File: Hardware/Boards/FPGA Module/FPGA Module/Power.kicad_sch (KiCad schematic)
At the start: 102 parts, among them Q2 IRLML6244, Q3 IRLML6244, Q4 IRLML6244, U10 INA700AYWFR, U12 INA700AYWFR, U2 INA700AYWFR, U22 TPSM33625RDNR, U23 TPSM33625RDNR, U24 TPSM33625RDNR, U3 AOZ2369QI-11, U4 TPS62933O, U7 INA700AYWFR, U8 INA236

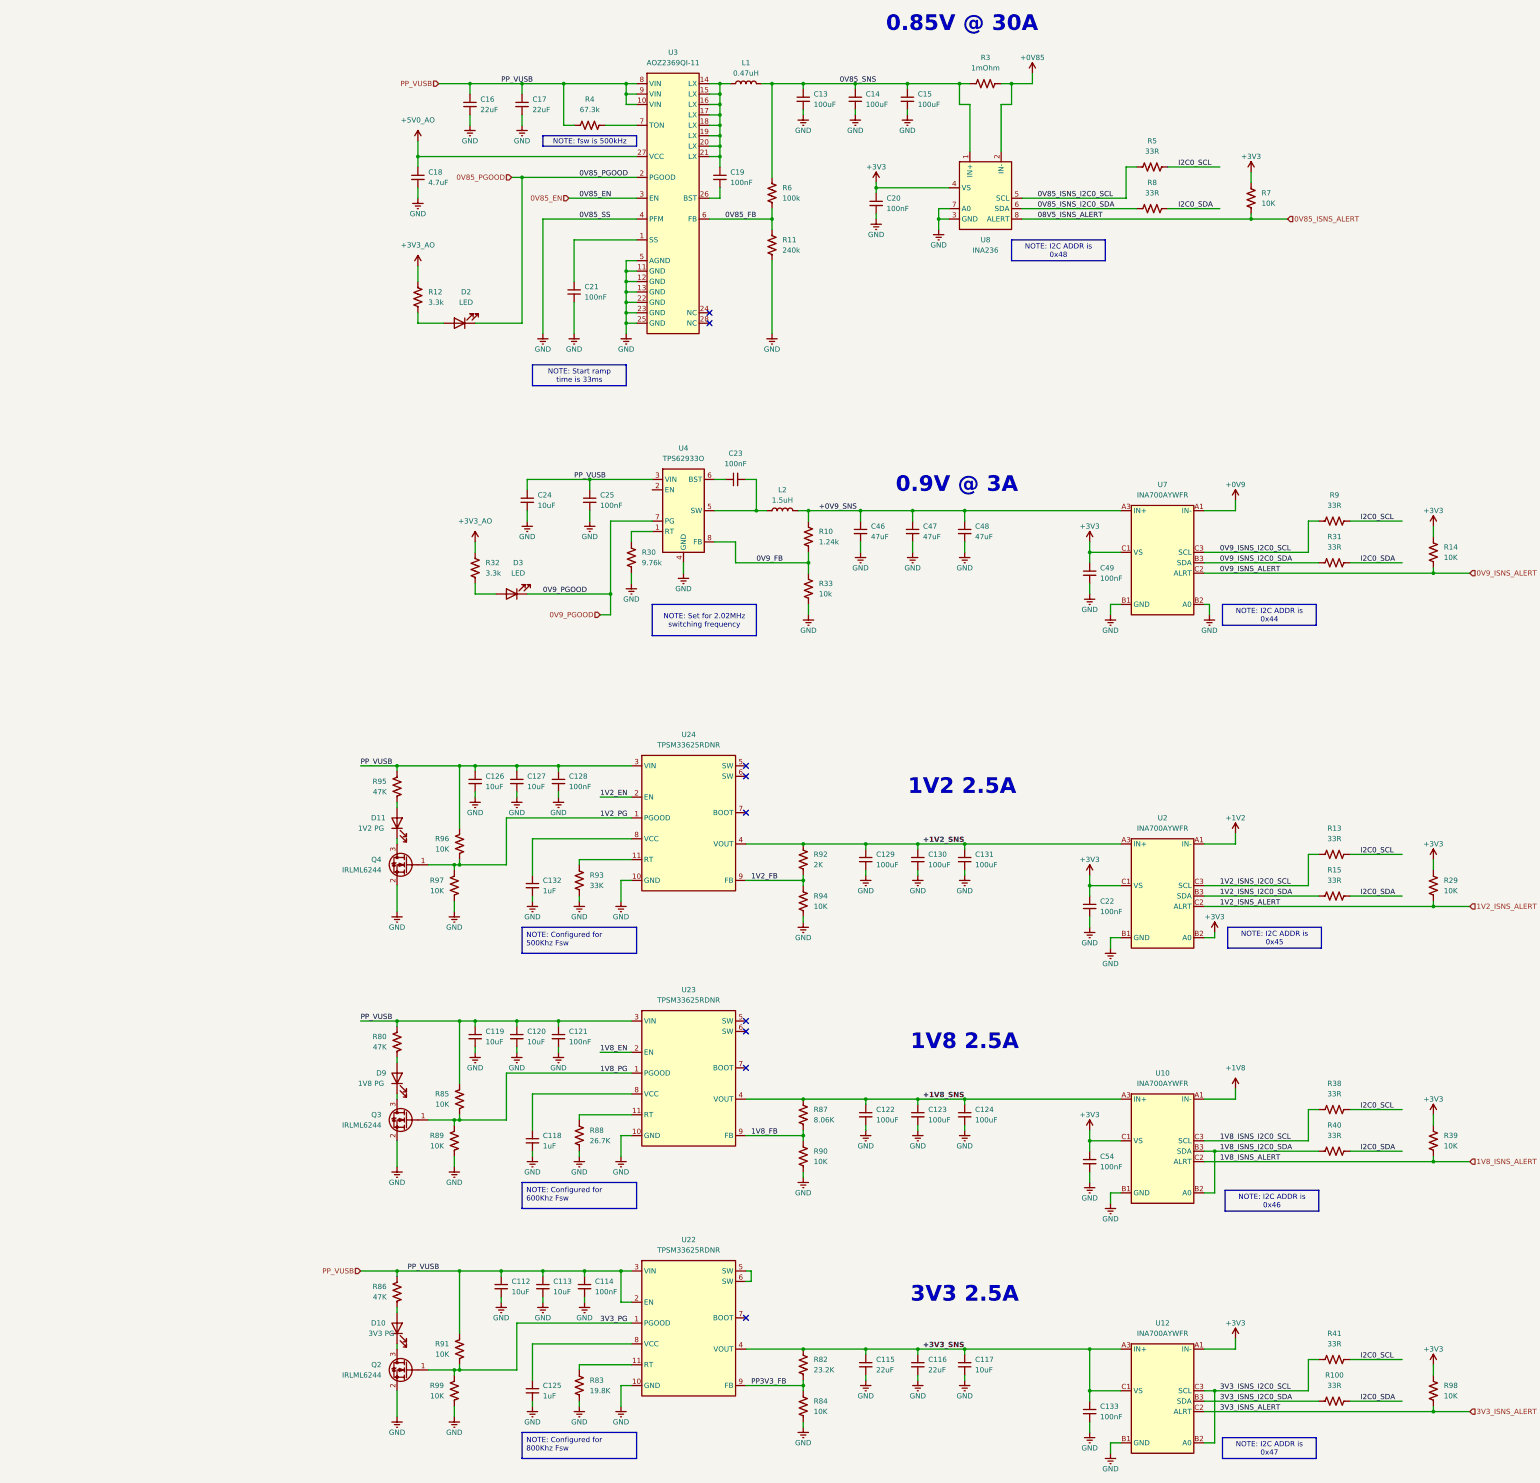
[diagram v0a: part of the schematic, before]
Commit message: updated fpga module schematics
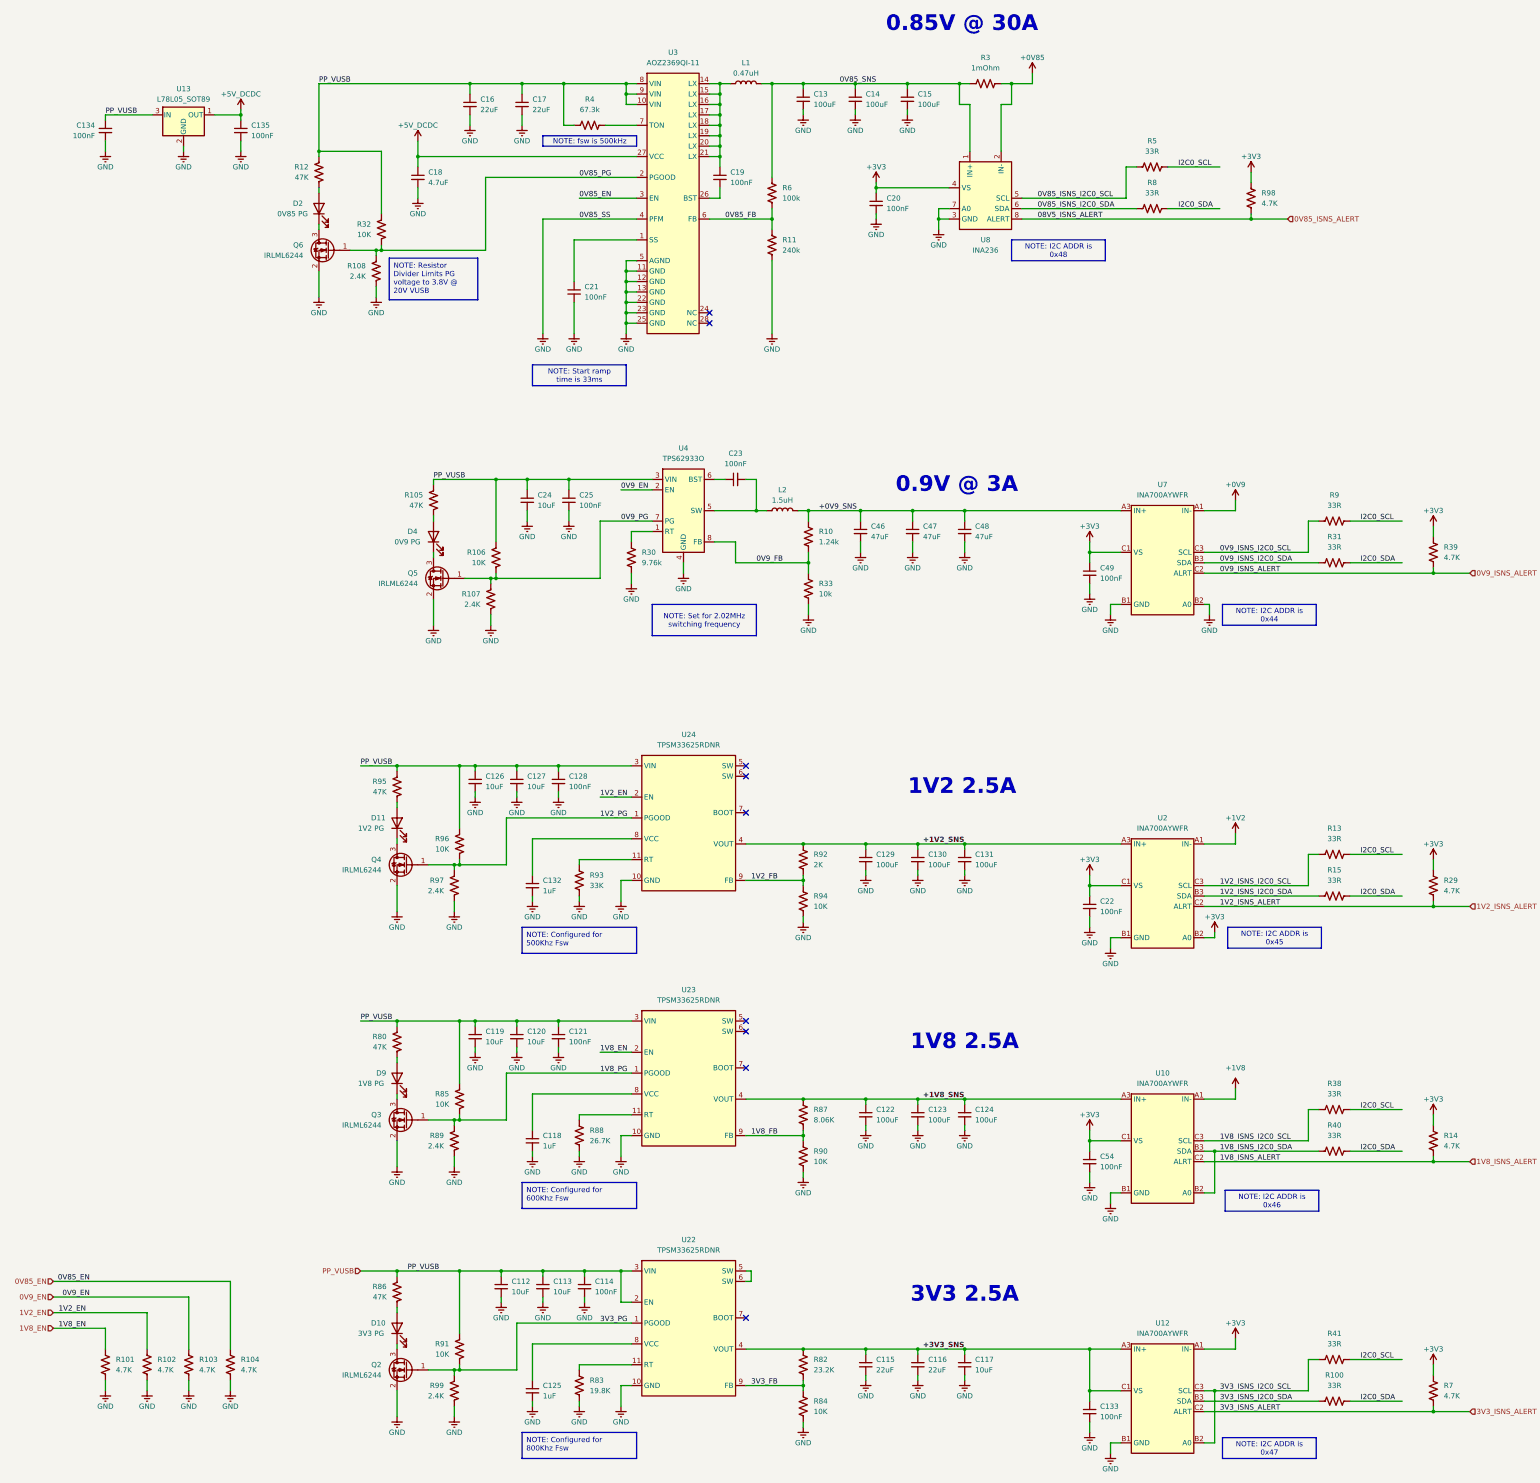
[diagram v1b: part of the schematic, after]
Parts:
- removed D3: LED, LED_SMD:LED_0603_1608Metric, symbol Device:LED
- added C134, C135: 100nF, Capacitor_SMD:C_0402_1005Metric, symbol Device:C_Small
- added D4: 0V9 PG, LED_SMD:LED_0603_1608Metric, symbol Device:LED
- added Q5, Q6: IRLML6244, Package_TO_SOT_SMD:SOT-23, symbol Transistor_FET:IRLML6244
- added R101, R102, R103, R104: 4.7K, Resistor_SMD:R_0402_1005Metric, symbol Device:R_US
- added R105: 47K, Resistor_SMD:R_0402_1005Metric, symbol Device:R_US
- added R106: 10K, Resistor_SMD:R_0402_1005Metric, symbol Device:R_US
- added R107, R108: 2.4K, Resistor_SMD:R_0402_1005Metric, symbol Device:R_US
- added U13: L78L05_SOT89, Package_TO_SOT_SMD:SOT-89-3, symbol Regulator_Linear:L78L05_SOT89
- D2: value LED -> 0V85 PG
- R12: value 3.3k -> 47K
- R14, R29, R39, R7, R98: value 10K -> 4.7K
- R32: value 3.3k -> 10K
- R89, R97, R99: value 10K -> 2.4K
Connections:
- net 0V85_EN: now also R104.2
- net 0V85_ISNS_ALERT: now also R98.1; no longer R7.1
- net 0V9_ISNS_ALERT: now also R39.1; no longer R14.1
- net 1V2_EN: now also R102.2
- net 1V8_EN: now also R101.2
- net 1V8_ISNS_ALERT: now also R14.1; no longer R39.1
- net 3V3_ISNS_ALERT: now also R7.1; no longer R98.1
- net GND: now also C134.2, C135.2, Q5.2 (S), Q6.2 (S), R101.1, R102.1, R103.1, R104.1, R107.1, R108.1, U13.2 (GND)
- net PP_VUSB: now also R12.2, R32.2, C134.1, R105.2, R106.2, U13.3 (IN)
- net at D2.2 (A): now also R12.1; no longer R12.2
- net 0V9_EN: now reaches U4.2 (EN)
- net 0V9_EN: now also R103.2
- net +3V3_AO renamed 0V85_PG
- net 0V85_PG: now also U3.2 (PGOOD), Q6.1 (G), R108.2; no longer R12.1
- net +5V0_AO renamed +5V_DCDC
- net +5V_DCDC: now also C135.1, U13.1 (OUT)
- net 0V85_PGOOD: no longer names the net of D2.1 (K)
- net 0V85_PGOOD: now also Q6.3 (D); no longer U3.2 (PGOOD)
- net 0V9_PGOOD renamed 0V9_PG
- net 0V9_PG: now also Q5.1 (G), R106.1, R107.2
- net PP3V3_FB renamed 3V3_FB
- new net: D4.1 (K), Q5.3 (D)
- new net: D4.2 (A), R105.1
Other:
- moved on the sheet: C25

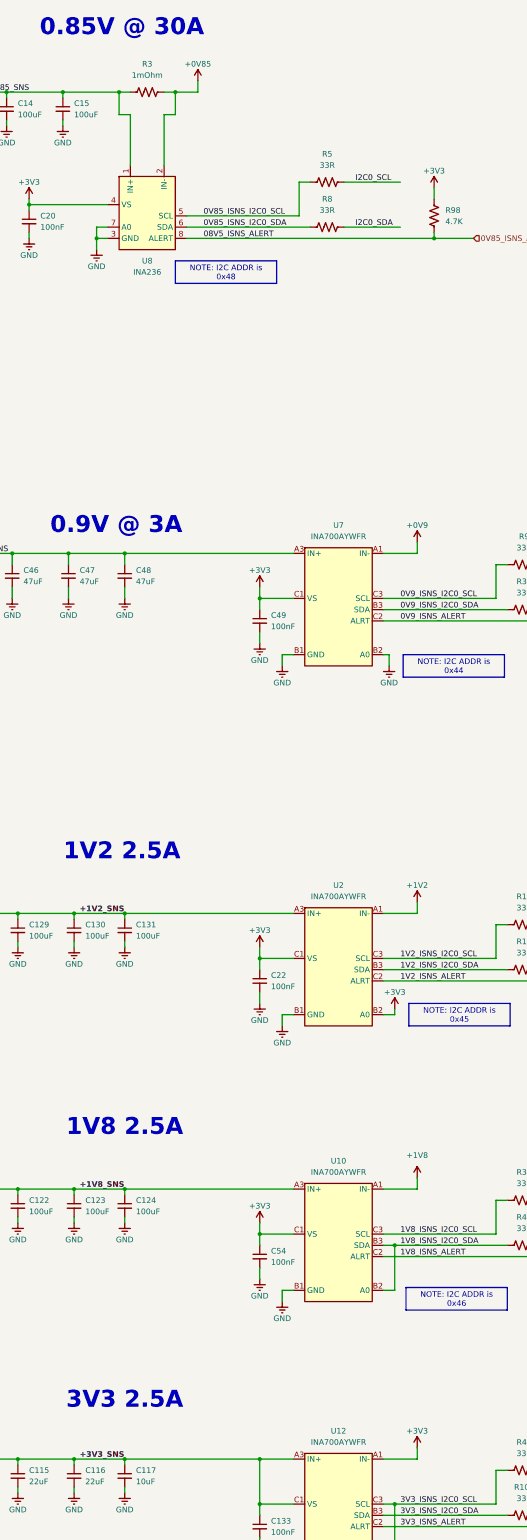
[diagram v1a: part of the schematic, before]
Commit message: Update FPGA Module Netclasses
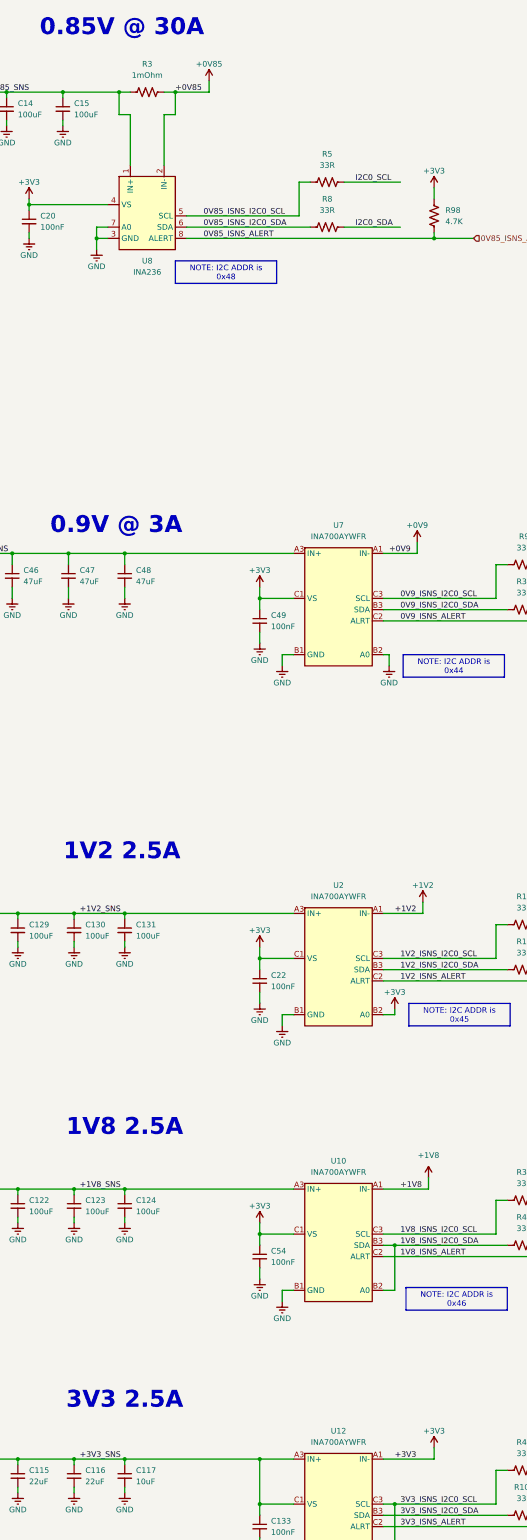
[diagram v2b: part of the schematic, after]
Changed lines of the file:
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@@
 	(wire
 		(pts
-			(xy 360.68 350.52) (xy 360.68 347.98)
+			(xy 364.49 350.52) (xy 364.49 347.98)
 		)
 		(stroke
@@
 	(wire
 		(pts
-			(xy 353.06 227.33) (xy 360.68 227.33)
+			(xy 353.06 227.33) (xy 361.95 227.33)
 		)
 		(stroke
@@
 	(wire
 		(pts
-			(xy 353.06 350.52) (xy 360.68 350.52)
+			(xy 353.06 350.52) (xy 364.49 350.52)
 		)
 		(stroke
@@
 	(wire
 		(pts
-			(xy 306.07 41.91) (xy 311.15 41.91)
+			(xy 306.07 41.91) (xy 313.69 41.91)
 		)
 		(stroke
@@
 	(wire
 		(pts
-			(xy 353.06 289.56) (xy 360.68 289.56)
+			(xy 353.06 289.56) (xy 363.22 289.56)
 		)
 		(stroke
@@
 	(wire
 		(pts
-			(xy 311.15 41.91) (xy 311.15 39.37)
+			(xy 313.69 41.91) (xy 313.69 39.37)
 		)
 		(stroke
@@
 	(wire
 		(pts
-			(xy 360.68 289.56) (xy 360.68 287.02)
+			(xy 363.22 289.56) (xy 363.22 287.02)
 		)
 		(stroke
@@
 	(wire
 		(pts
-			(xy 360.68 227.33) (xy 360.68 224.79)
+			(xy 361.95 227.33) (xy 361.95 224.79)
 		)
 		(stroke
@@
 		)
 	)
+	(label "+0V85"
+		(at 306.07 41.91 0)
+		(fields_autoplaced yes)
+		(effects
+			(font
+				(size 1.27 1.27)
+			)
+			(justify left bottom)
+		)
+	)
 	(label "1V2_ISNS_I2C0_SDA"
 		(at 356.87 240.03 0)
@@
 		)
 	)
+	(label "+1V2"
+		(at 355.6 227.33 0)
+		(fields_autoplaced yes)
+		(effects
+			(font
+				(size 1.27 1.27)
+			)
+			(justify left bottom)
+		)
+	)
 	(label "1V8_ISNS_ALERT"
 		(at 356.87 304.8 0)
@@
 			(font
 				(size 1.27 1.27)
-				(bold yes)
 			)
 			(justify left bottom)
@@
 		)
 	)
-	(label "08V5_ISNS_ALERT"
+	(label "0V85_ISNS_ALERT"
 		(at 312.42 74.93 0)
 		(fields_autoplaced yes)
@@
 		)
 	)
+	(label "+0V9"
+		(at 354.33 146.05 0)
+		(fields_autoplaced yes)
+		(effects
+			(font
+				(size 1.27 1.27)
+			)
+			(justify left bottom)
+		)
+	)
 	(label "3V3_ISNS_I2C0_SDA"
 		(at 356.87 363.22 0)
@@
 			(font
 				(size 1.27 1.27)
-				(bold yes)
 			)
 			(justify left bottom)
@@
 		)
 	)
+	(label "+3V3"
+		(at 355.6 350.52 0)
+		(fields_autoplaced yes)
+		(effects
+			(font
+				(size 1.27 1.27)
+			)
+			(justify left bottom)
+		)
+	)
 	(label "1V2_ISNS_ALERT"
 		(at 356.87 242.57 0)
@@
 			(font
 				(size 1.27 1.27)
-				(bold yes)
 			)
 			(justify left bottom)
@@
 		)
 	)
+	(label "+1V8"
+		(at 356.87 289.56 0)
+		(fields_autoplaced yes)
+		(effects
+			(font
+				(size 1.27 1.27)
+			)
+			(justify left bottom)
+		)
+	)
 	(hierarchical_label "1V8_ISNS_ALERT"
 		(shape input)
@@
 	(symbol
 		(lib_id "power:VAA")
-		(at 311.15 39.37 0)
+		(at 313.69 39.37 0)
 		(unit 1)
 		(exclude_from_sim no)
@@
 		(dnp no)
 		(property "Reference" "#PWR020"
-			(at 311.15 43.18 0)
+			(at 313.69 43.18 0)
 			(effects
 				(font
@@
 		)
 		(property "Value" "+0V85"
-			(at 311.15 35.56 0)
+			(at 313.69 35.56 0)
 			(effects
 				(font
@@
 		)
 		(property "Footprint" ""
-			(at 311.15 39.37 0)
+			(at 313.69 39.37 0)
 			(effects
 				(font
@@
 		)
 		(property "Datasheet" ""
-			(at 311.15 39.37 0)
+			(at 313.69 39.37 0)
 			(effects
 				(font
@@
 		)
 		(property "Description" "Power symbol creates a global label with name \"VAA\""
-			(at 311.15 39.37 0)
+			(at 313.69 39.37 0)
 			(effects
 				(font
@@
 	(symbol
 		(lib_id "power:+3V3")
-		(at 360.68 347.98 0)
+		(at 364.49 347.98 0)
 		(unit 1)
 		(exclude_from_sim no)
@@
 		(dnp no)
 		(property "Reference" "#PWR0208"
-			(at 360.68 351.79 0)
+			(at 364.49 351.79 0)
 			(effects
 				(font
@@
 		)
 		(property "Value" "+3V3"
-			(at 360.68 344.17 0)
+			(at 364.49 344.17 0)
 			(effects
 				(font
@@
 		)
 		(property "Footprint" ""
-			(at 360.68 347.98 0)
+			(at 364.49 347.98 0)
 			(effects
 				(font
@@
 		)
 		(property "Datasheet" ""
-			(at 360.68 347.98 0)
+			(at 364.49 347.98 0)
 			(effects
 				(font
@@
 		)
 		(property "Description" "Power symbol creates a global label with name \"+3V3\""
-			(at 360.68 347.98 0)
+			(at 364.49 347.98 0)
 			(effects
 				(font
@@
 	(symbol
 		(lib_id "power:+1V8")
-		(at 360.68 287.02 0)
+		(at 363.22 287.02 0)
 		(unit 1)
 		(exclude_from_sim no)
@@
 		(fields_autoplaced yes)
 		(property "Reference" "#PWR0220"
-			(at 360.68 290.83 0)
+			(at 363.22 290.83 0)
 			(effects
 				(font
@@
 		)
 		(property "Value" "+1V8"
-			(at 360.68 281.94 0)
+			(at 363.22 281.94 0)
 			(effects
 				(font
@@
 		)
 		(property "Footprint" ""
-			(at 360.68 287.02 0)
+			(at 363.22 287.02 0)
 			(effects
 				(font
@@
 		)
 		(property "Datasheet" ""
-			(at 360.68 287.02 0)
+			(at 363.22 287.02 0)
 			(effects
 				(font
@@
 		)
 		(property "Description" "Power symbol creates a global label with name \"+1V8\""
-			(at 360.68 287.02 0)
+			(at 363.22 287.02 0)
 			(effects
 				(font
@@
 	(symbol
 		(lib_id "power:+1V2")
-		(at 360.68 224.79 0)
+		(at 361.95 224.79 0)
 		(unit 1)
 		(exclude_from_sim no)
@@
 		(dnp no)
 		(property "Reference" "#PWR021"
-			(at 360.68 228.6 0)
+			(at 361.95 228.6 0)
 			(effects
 				(font
@@
 		)
 		(property "Value" "+1V2"
-			(at 360.68 220.98 0)
+			(at 361.95 220.98 0)
 			(effects
 				(font
@@
 		)
 		(property "Footprint" ""
-			(at 360.68 224.79 0)
+			(at 361.95 224.79 0)
 			(effects
 				(font
@@
 		)
 		(property "Datasheet" ""
-			(at 360.68 224.79 0)
+			(at 361.95 224.79 0)
 			(effects
 				(font
@@
 		)
 		(property "Description" "Power symbol creates a global label with name \"+1V2\""
-			(at 360.68 224.79 0)
+			(at 361.95 224.79 0)
 			(effects
 				(font
